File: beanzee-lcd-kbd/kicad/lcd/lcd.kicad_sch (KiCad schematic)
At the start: 6 parts, among them U1 74LS138, U3 74LS04

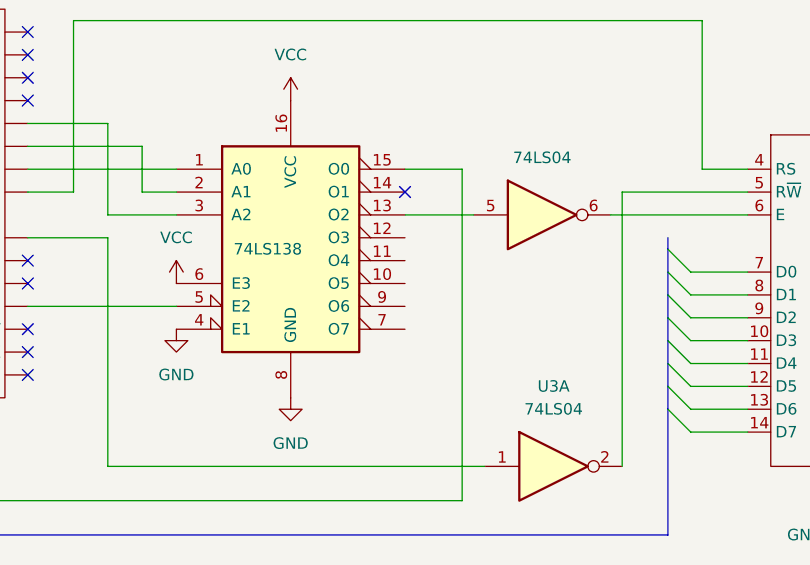
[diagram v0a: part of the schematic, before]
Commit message: update lcd schematic
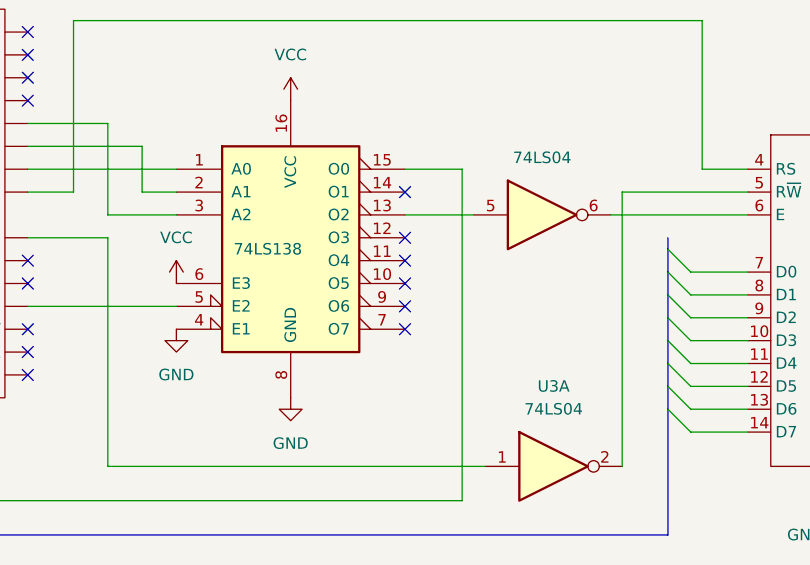
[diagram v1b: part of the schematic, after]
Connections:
- no-connect marks 23 -> 28
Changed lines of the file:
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@@
   (junction (at 166.37 12.7) (diameter 0) (color 0 0 0 0)
   )
+  (no_connect (at 113.03 34.29))
   (no_connect (at 30.48 54.61))
   (no_connect (at 71.12 36.83))
   (no_connect (at 27.94 54.61))
   (no_connect (at 71.12 13.97))
+  (no_connect (at 113.03 41.91))
   (no_connect (at 71.12 39.37))
   (no_connect (at 58.42 6.35))
@@
   (no_connect (at 71.12 19.05))
   (no_connect (at 71.12 49.53))
+  (no_connect (at 113.03 39.37))
+  (no_connect (at 113.03 44.45))
   (no_connect (at 43.18 54.61))
   (no_connect (at 53.34 6.35))
@@
   (no_connect (at 71.12 46.99))
   (no_connect (at 113.03 29.21))
+  (no_connect (at 113.03 36.83))
   (no_connect (at 50.8 6.35))
   (no_connect (at 45.72 6.35))
